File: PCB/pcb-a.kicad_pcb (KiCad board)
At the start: 2 copper layers, 109.7 x 43.5 mm, 45 parts, among them Q1 BC327, Q3 BC337, SW1 config, U1 MCP23008-xP, U2 MAX232I, U4 ATmega16L-8P, Y1 8Mhz

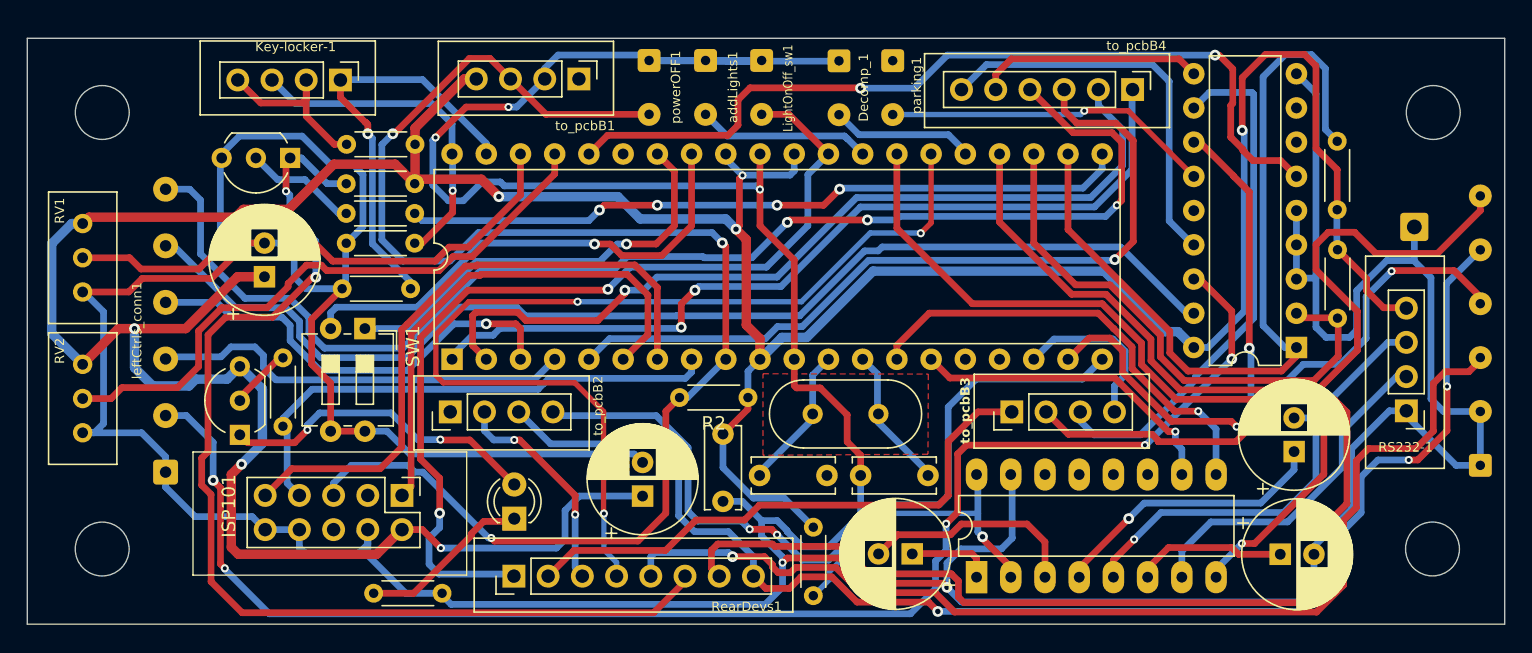
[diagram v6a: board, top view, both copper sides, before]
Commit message: o_NEUTRAL is connected directly to the led
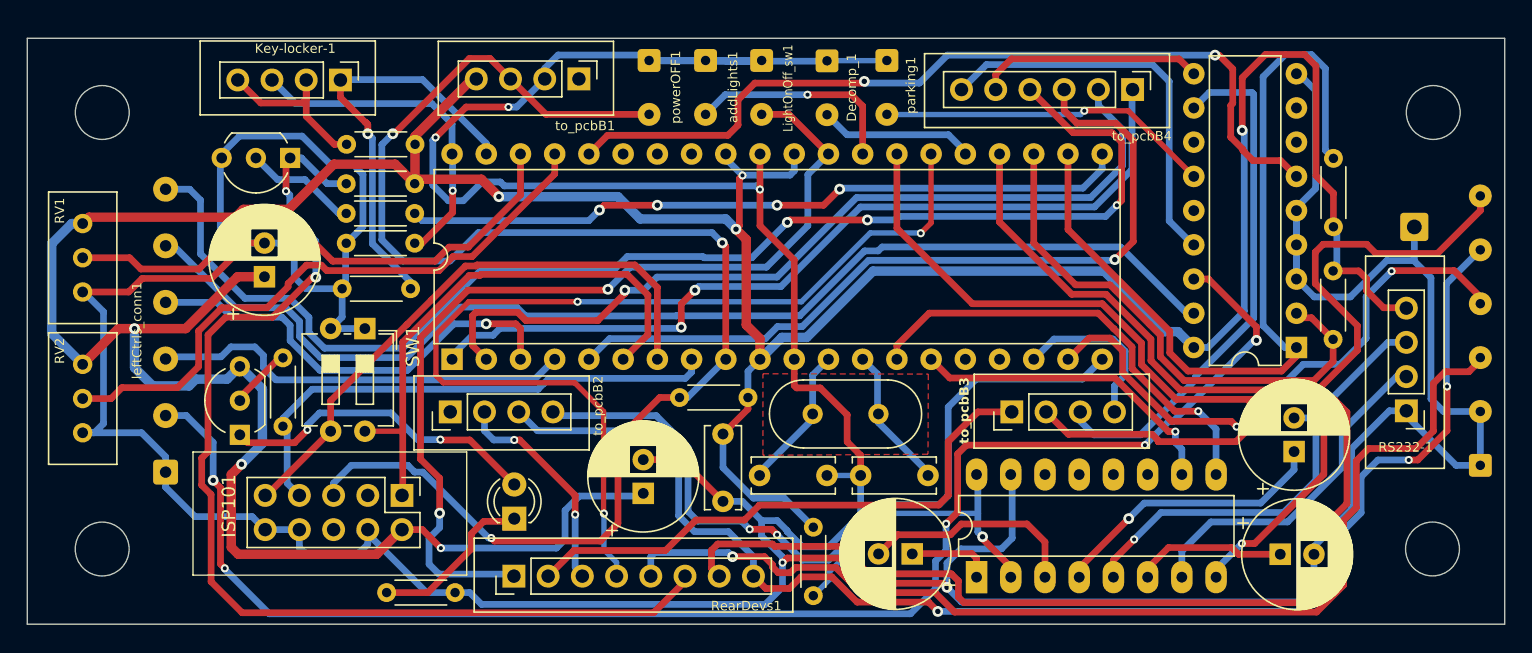
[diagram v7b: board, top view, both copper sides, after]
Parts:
- moved R5 1.61 mm to (199.3, 77.9)
- moved R10 1.30 mm to (199.3, 74.6)
- moved R9 0.97 mm to (129.0, 101.8)
- moved Decomp_1 0.89 mm to (161.7, 62.3)
- moved parking1 0.43 mm to (166.1, 62.3)
- moved C7 0.21 mm to (148.1, 94.4)
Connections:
- RearDevs1 pad 7: i_neutral -> c_neutral
- SW1 pad 1: Net-(U4-PA6) -> GND
- SW1 pad 2: Net-(U4-PA7) -> GND
- SW1 pad 3: GND -> Net-(ISP101-Pin_9)
- SW1 pad 4: GND -> Net-(ISP101-Pin_1)
- U1 pad 12: o_neutral -> unconnected-(U1-GP2-Pad12)
- U4 pad 27: i_neutral -> c_neutral
- U4 pad 33: Net-(U4-PA7) -> unconnected-(U4-PA7-Pad33)
- U4 pad 34: Net-(U4-PA6) -> unconnected-(U4-PA6-Pad34)
- to_pcbB3 pad 2: o_neutral -> c_neutral
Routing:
- net c_neutral: track 0.00 -> 128.8 mm
- net i_neutral: track 110.2 -> 0.00 mm
- net o_neutral: track 39.8 -> 0.00 mm, vias 2 -> 0
- net Net-(U4-PA7): track 36.7 -> 0.00 mm, vias 1 -> 0
- net Net-(U4-PA6): track 32.0 -> 0.00 mm, vias 1 -> 0
- net GND: track 432.4 -> 408.7 mm
- net Net-(ISP101-Pin_9): track 47.3 -> 43.5 mm
- net i_addLight: track 12.9 -> 16.2 mm, vias 0 -> 1
- net Net-(ISP101-Pin_1): track 37.9 -> 40.7 mm
- net i_leftArrow: track 110.4 -> 112.5 mm
- net Net-(U1-SDA): track 41.2 -> 39.7 mm
- net Net-(U1-SCL): track 62.7 -> 63.9 mm
- net tempPower: track 281.2 -> 282.3 mm
- net i_engineON: track 63.7 -> 62.7 mm
- net i_decompr: track 10.7 -> 11.6 mm
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
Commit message: No USB support and PCB-B size reducing
Implementing USB power support using 7805 was a stupid idea: too much wasted electic current in Joule effect. So, I moved just
one 7805 in the PCB-A, because the its used power is very low. It allowed me to optimize the PCB-B used space and reduce its
whole size ;-)
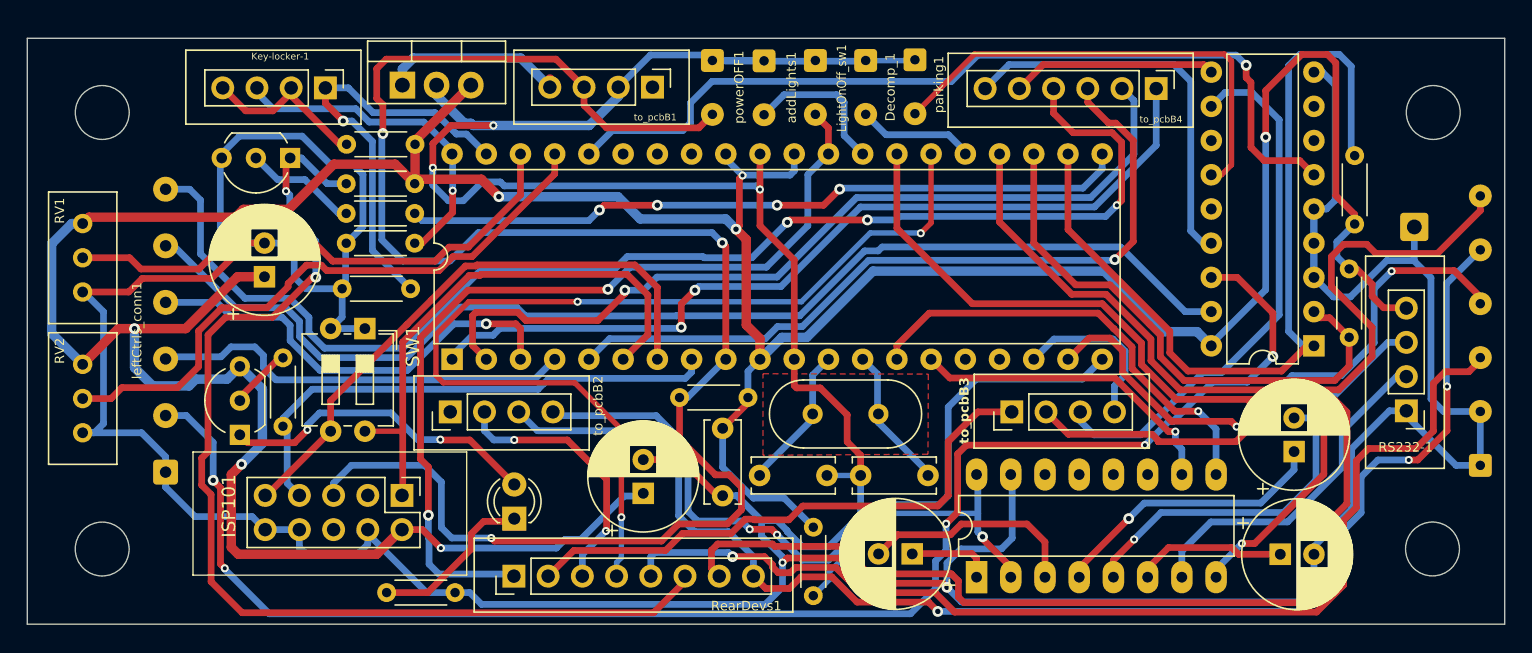
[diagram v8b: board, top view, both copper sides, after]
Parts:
- added U3: L7805, Package_TO_SOT_THT:TO-220-3_Vertical, F.Cu at (130.2, 64.1)
- moved to_pcbB1 5.49 mm to (148.8, 64.3)
- moved powerOFF1 4.70 mm to (153.2, 62.3)
- moved addLights1 4.34 mm to (157.0, 62.3)
- moved LightOnOff_sw1 3.99 mm to (160.8, 62.3)
- moved Decomp_1 2.87 mm to (164.6, 62.3)
- moved parking1 2.08 mm to (168.2, 62.2)
- moved to_pcbB4 1.75 mm to (186.1, 64.4)
- moved R10 1.59 mm to (200.9, 74.4)
- moved U1 1.30 mm to (197.8, 83.5)
- moved Key-locker-1 1.26 mm to (124.5, 64.3)
- moved R5 1.20 mm to (200.5, 77.8)
- moved C2 0.42 mm to (154.0, 89.6)
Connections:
- C1 pad 1: tempPower -> 5V
- C2 pad 1: tempPower -> 5V
- C7 pad 1: tempPower -> 5V
- ISP101 pad 2: tempPower -> 5V
- Q1 pad 3: tempPower -> 5V
- R1 pad 1: tempPower -> 5V
- R10 pad 1: tempPower -> 5V
- R11 pad 1: tempPower -> 5V
- R2 pad 1: tempPower -> 5V
- R5 pad 1: tempPower -> 5V
- R6 pad 2: tempPower -> 5V
- RS232-1 pad 4: tempPower -> 5V
- RV1 pad 1: tempPower -> 5V
- RV2 pad 1: tempPower -> 5V
- U1 pad 18: tempPower -> 5V
- U4 pad 10: tempPower -> 5V
- U4 pad 30: tempPower -> 5V
- U4 pad 32: tempPower -> 5V
- to_pcbB1 pad 4: tempPower -> Net-(U3-IN)
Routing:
- net tempPower: track 282.3 -> 0.00 mm, vias 7 -> 0
- net 5V: track 0.00 -> 279.6 mm, vias 0 -> 7
- net i_powerOFF: track 109.3 -> 129.8 mm
- net Net-(U3-IN): track 0.00 -> 14.0 mm
- net i_parking: track 24.9 -> 35.1 mm, vias 1 -> 0
- net GND: track 408.7 -> 403.2 mm
- net i_addLight: track 16.2 -> 11.2 mm, vias 1 -> 0
- net c_rightArrow: track 16.3 -> 19.9 mm
- net c_rearLight: track 68.7 -> 65.2 mm
- net i_decompr: track 11.6 -> 8.72 mm
- net i_leftArrow: track 112.5 -> 115.0 mm
- net o_addLight: track 59.1 -> 57.1 mm
- net o_rightArrow: track 16.8 -> 15.2 mm
- net Net-(U1-SDA): track 39.7 -> 41.2 mm
- net i_rightArrow: track 86.4 -> 87.7 mm
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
